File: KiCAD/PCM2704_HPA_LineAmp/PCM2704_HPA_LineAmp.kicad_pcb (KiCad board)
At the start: 2 copper layers, 33 parts, among them J1 HPA_L, J10 PCM2704Board, J11 USB_LED, J2 LINE_L, J3 HPA_R, J4 LINE_R, J5 PWR_IN, J6 PWR_OUT, J7 PWR_OUT, J8 TP_GND, J9 PWR_LED, U1 NJM4580

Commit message: Update: PCM2704_HPA_LineAmp board design
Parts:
- added J12: PWR-, Connector_JST:JST_XH_B2B-XH-A_1x02_P2.50mm_Vertical, F.Cu at (119.4, 114.3)
- added REF**: MountingHole_3.2mm_M3, MountingHole:MountingHole_3.2mm_M3, F.Cu at (116.8, 48.3)
- added REF**: MountingHole_3.2mm_M3, MountingHole:MountingHole_3.2mm_M3, F.Cu at (182.9, 48.3)
- added REF**: MountingHole_3.2mm_M3, MountingHole:MountingHole_3.2mm_M3, F.Cu at (182.9, 137.2)
- added REF**: MountingHole_3.2mm_M3, MountingHole:MountingHole_3.2mm_M3, F.Cu at (116.8, 137.2)
- C4: footprint Capacitor_THT:C_Disc_D3.0mm_W1.6mm_P2.50mm -> Capacitor_THT:C_Disc_D4.3mm_W1.9mm_P5.00mm
- C5, C6: footprint Capacitor_THT:CP_Radial_D8.0mm_P5.00mm -> Capacitor_THT:CP_Radial_D7.5mm_P2.50mm
- CRD1, CRD2: footprint Diode_THT:D_A-405_P7.62mm_Horizontal -> Diode_THT:D_DO-35_SOD27_P7.62mm_Horizontal
- J5: value PWR_IN -> PWR+; footprint Connector_JST:JST_XH_B3B-XH-A_1x03_P2.50mm_Vertical -> Connector_JST:JST_XH_B2B-XH-A_1x02_P2.50mm_Vertical
- moved R1 67.9 mm to (147.3, 58.4), turned to 90 degrees
- moved D1 65.5 mm to (129.5, 127.0), turned to 90 degrees
- moved CRD2 61.5 mm to (177.8, 50.8), turned to 270 degrees
- moved J1 60.2 mm to (119.4, 55.9), turned to 90 degrees
- moved J10 59.5 mm to (160.0, 48.3)
- moved C7 55.9 mm to (157.5, 63.5), turned to 90 degrees
- moved J7 55.6 mm to (172.7, 119.4), turned to 90 degrees
- moved J6 53.5 mm to (162.6, 119.4), turned to 90 degrees
- moved J2 52.6 mm to (119.4, 66.0), turned to 90 degrees
- moved J5 50.6 mm to (119.4, 124.5), turned to 90 degrees
- moved J8 49.7 mm to (177.8, 96.5), turned to 90 degrees
- moved R7 49.2 mm to (157.5, 83.8), turned to 180 degrees
- moved J3 47.9 mm to (119.4, 76.2), turned to 90 degrees
- moved C3 46.7 mm to (129.5, 66.0), turned to 270 degrees
- moved C5 43.6 mm to (149.8, 63.5), turned to 180 degrees
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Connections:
- D1 pad 1: GND -> Net-(D1-Pad1)
- D1 pad 2: Net-(D1-Pad2) -> +9V
- R5 pad 1: +9V -> Net-(D1-Pad1)
- R5 pad 2: Net-(D1-Pad2) -> GND
- U1 pad 1: Net-(J1-Pad1) -> Net-(J3-Pad1)
- U1 pad 2: Net-(J1-Pad1) -> Net-(J3-Pad1)
- U1 pad 3: Net-(C5-Pad2) -> Net-(C6-Pad2)
- U1 pad 5: Net-(C6-Pad2) -> Net-(C5-Pad2)
- U1 pad 6: Net-(J3-Pad1) -> Net-(J1-Pad1)
- U1 pad 7: Net-(J3-Pad1) -> Net-(J1-Pad1)
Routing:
- net GND: track 0.00 -> 334.4 mm
- net +9V: track 0.00 -> 125.1 mm, vias 0 -> 4
- net -9V: track 0.00 -> 123.5 mm
- net Net-(J1-Pad1): track 0.00 -> 37.7 mm
- net Net-(J3-Pad1): track 0.00 -> 29.6 mm
- net Net-(CRD2-Pad1): track 0.00 -> 19.9 mm
- net Net-(C6-Pad2): track 0.00 -> 18.8 mm
- net Net-(C5-Pad2): track 0.00 -> 13.8 mm
- net Net-(C6-Pad1): track 0.00 -> 10.2 mm
- net Net-(C5-Pad1): track 0.00 -> 10.2 mm
- net Net-(D2-Pad2): track 0.00 -> 6.13 mm
- net Net-(C8-Pad2): track 0.00 -> 5.16 mm
- net Net-(C7-Pad2): track 0.00 -> 5.16 mm
- net +5V: track 0.00 -> 5.08 mm
- net Net-(D1-Pad1): track 0.00 -> 5.08 mm
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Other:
- board outline added: 71.1 x 94 mm

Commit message: Update: PCM2704_HPA_LineAmp board design
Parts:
- removed CRD2: 1mA, Diode_THT:D_DO-35_SOD27_P7.62mm_Horizontal
- removed the R5 at (134.6, 127.0)
- removed REF** (x4): MountingHole_3.2mm_M3, MountingHole:MountingHole_3.2mm_M3
- added R10: 3k3, Resistor_THT:R_Axial_DIN0204_L3.6mm_D1.6mm_P7.62mm_Horizontal, F.Cu at (180.3, 50.8)
- added R6: 15, Resistor_THT:R_Axial_DIN0204_L3.6mm_D1.6mm_P7.62mm_Horizontal, F.Cu at (154.9, 83.8)
- CRD1: value 1mA -> 5mA
- R1, R2: value 330 -> 3k3
- R7: value 15 -> 10k
- moved R7 48.8 mm to (127.0, 121.9), turned to 0 degrees
- moved J12 5.08 mm to (180.3, 61.0), turned to 0 degrees
- moved D1 3.59 mm to (127.0, 124.5), turned to 270 degrees
- moved C4 2.54 mm to (139.7, 68.6)
- moved U1 2.54 mm to (129.5, 73.7)
- moved J1 2.54 mm to (119.4, 127.0)
- moved J8 2.54 mm to (172.7, 121.9)
- moved R8 2.54 mm to (134.6, 116.8), turned to 180 degrees
- moved C1 2.54 mm to (144.8, 129.5)
- moved C3 2.54 mm to (127.0, 66.0)
- moved C5 2.54 mm to (147.3, 63.5)
- moved C6 2.54 mm to (147.3, 73.7)
- moved C7 2.54 mm to (154.9, 63.5)
- moved C8 2.54 mm to (154.9, 73.7)
- moved D2 2.54 mm to (127.0, 111.8), turned to 270 degrees
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- renumbered J5 to J1, J9 to J10, J8 to J11, J11 to J12, J12 to J2, J1 to J3, J2 to J4, J3 to J5, J4 to J6, J6 to J7, J7 to J8, J10 to J9, R6 to R5
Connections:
- R7 pad 1: Net-(C8-Pad2) -> Net-(D1-Pad1)
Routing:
- net GND: track 334.4 -> 342.7 mm
- net Net-(J3-Pad1): track 37.7 -> 30.5 mm
- net +9V: track 125.1 -> 131.8 mm
- net Net-(J12-Pad1): track 19.9 -> 13.8 mm
- net Net-(D2-Pad2): track 6.13 -> 2.54 mm
- net Net-(J5-Pad1): track 29.6 -> 26.4 mm
- net Net-(D1-Pad1): track 5.08 -> 2.54 mm
- net Net-(C6-Pad1): track 10.2 -> 12.7 mm
- net Net-(C5-Pad1): track 10.2 -> 12.7 mm
- net +5V: track 5.08 -> 7.62 mm

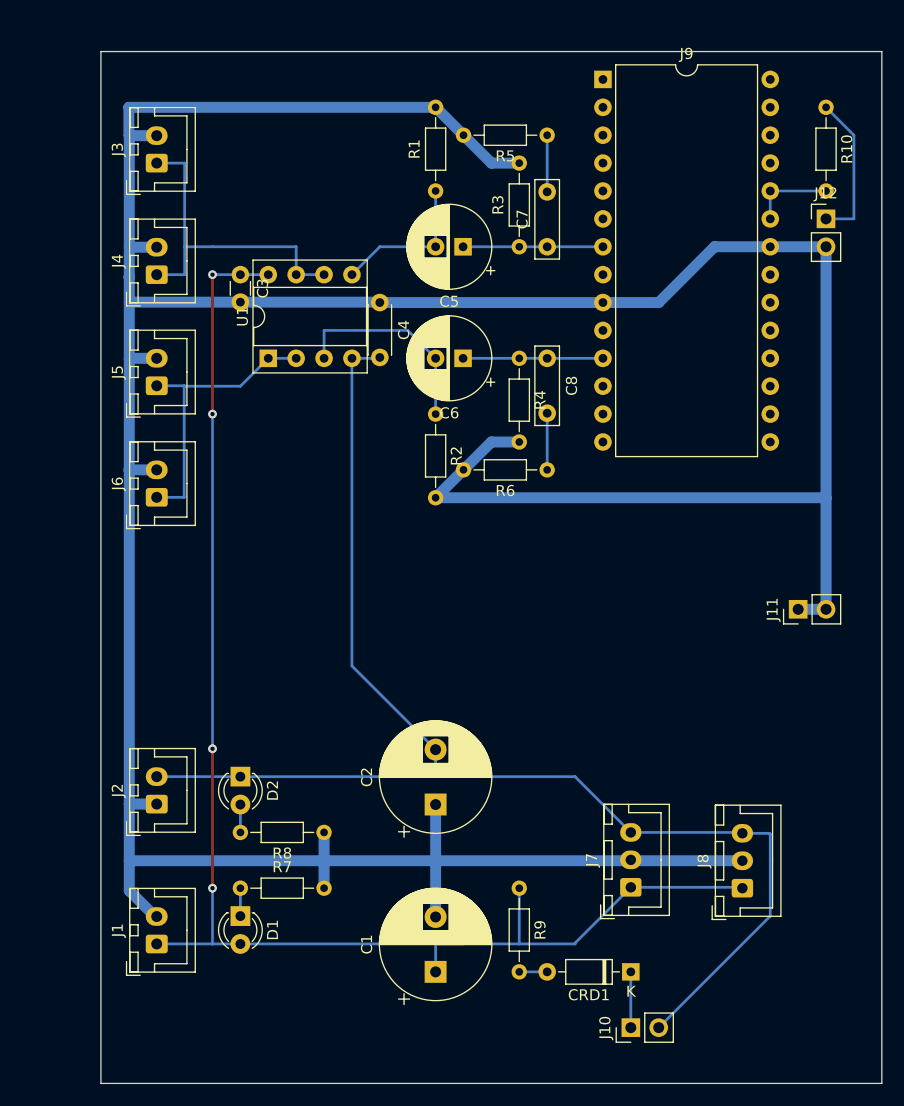
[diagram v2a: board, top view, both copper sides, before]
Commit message: Add: Case design
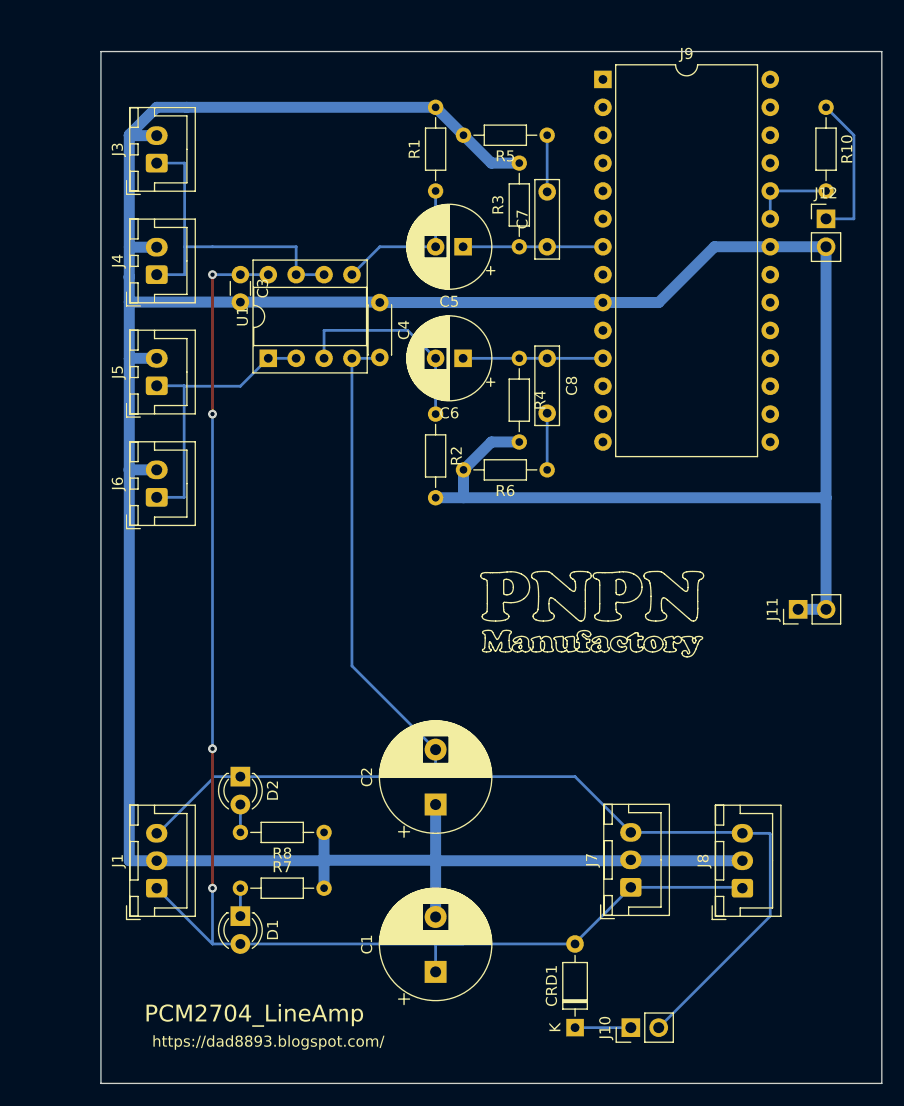
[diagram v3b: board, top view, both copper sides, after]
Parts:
- removed J2: PWR-, Connector_JST:JST_XH_B2B-XH-A_1x02_P2.50mm_Vertical
- removed R9: 10k, Resistor_THT:R_Axial_DIN0204_L3.6mm_D1.6mm_P7.62mm_Horizontal
- J1: value PWR+ -> PWR_IN; footprint Connector_JST:JST_XH_B2B-XH-A_1x02_P2.50mm_Vertical -> Connector_JST:JST_XH_B3B-XH-A_1x03_P2.50mm_Vertical
- R7, R8: value 10k -> 4k7
- moved CRD1 7.18 mm to (157.5, 134.6), turned to 90 degrees
- moved J1 5.08 mm to (119.4, 121.9)
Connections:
- CRD1 pad 2: Net-(CRD1-Pad2) -> +9V
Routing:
- net GND: track 342.7 -> 331.7 mm
- net +9V: track 131.8 -> 128.8 mm
- net Net-(CRD1-Pad2): track 2.54 -> 0.00 mm
- net -9V: track 123.7 -> 126.0 mm
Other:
- board text added: "PCM2704_LineAmp"
- board text added: "https://dad8893.blogspot.com/"
